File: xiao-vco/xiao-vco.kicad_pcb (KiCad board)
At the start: 2 copper layers, 38 x 100 mm, 52 parts, among them J1 C2M, J2 C2F, J3 Eurorack Power, J4 CV1, J5 V/OCT, J6 OUT, J7 CV2, J8 C1M, J9 C1F, U1 SeeeduinoXIAO, U2 MCP6004, U3 LM4040DBZ-10, U4 TL072, U5 LM1117-5.0

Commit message: First completed routing
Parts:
- removed the mouse-bite-2mm-slot at (169.0, 100.0)
- RV1: footprint Potentiometer_THT:Potentiometer_Alpha_RD901F-40-00D_Single_Vertical -> Personal:Potentiometer_Alpha_RD901F-40-00D_Single_Vertical-Hanging
- mouse-bite-2mm-slot (x2): footprint Panelization:mouse-bite-2mm-slot -> Personal:Mouse_bite_2x5mm
- moved R11 31.7 mm to (179.0, 121.5), turned to 180 degrees
- moved C6 13.2 mm to (184.8, 89.3), turned to -90 degrees
- moved C10 9.54 mm to (175.9, 86.9), turned to 0 degrees
- moved R9 8.02 mm to (175.1, 100.2), turned to 0 degrees
- moved C8 6.49 mm to (175.1, 97.9), turned to 0 degrees
- moved U4 6.10 mm to (176.9, 92.3), turned to 90 degrees
- moved mouse-bite-2mm-slot 6.00 mm to (169.0, 60.0)
- moved mouse-bite-2mm-slot 5.00 mm to (169.0, 140.0)
- moved R5 4.81 mm to (178.7, 100.2), turned to 180 degrees
- moved C7 4.13 mm to (182.5, 125.3), turned to -90 degrees
- moved C11 3.18 mm to (181.2, 94.3), turned to -90 degrees
- moved R4 2.25 mm to (175.3, 125.3)
- moved R8 2.15 mm to (178.7, 97.9), turned to 0 degrees
- moved U3 0.60 mm to (178.9, 125.3), turned to 180 degrees
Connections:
- C1 pad 2: GND -> GND1
- C2 pad 2: GND -> GND1
- C3 pad 2: GND -> GND1
- C4 pad 2: GND -> GND1
- J2 pad 1: GND -> GND1
- J4 pad S: GND -> GND1
- J5 pad S: GND -> GND1
- J6 pad S: GND -> GND1
- J7 pad S: GND -> GND1
- J9 pad 1: GND -> GND1
- RV1 pad 1: GND -> GND1
- RV2 pad 1: GND -> GND1
- RV3 pad 1: GND -> GND1
- RV4 pad 1: GND -> GND1
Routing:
- net +12V: track 0.07 -> 95.2 mm, vias 0 -> 1
- net -12V: track 2.18 -> 65.6 mm
- net +3V3: track 15.6 -> 58.4 mm, vias 0 -> 1
- net /CV1_IN: track 7.09 -> 44.1 mm, vias 0 -> 1
- net Net-(C8-Pad1): track 0.00 -> 36.4 mm, vias 0 -> 2
- net /CV2_IN: track 8.94 -> 43.1 mm, vias 0 -> 1
- net /AUDIO_OUT: track 0.00 -> 31.6 mm, vias 0 -> 1
- net +5V: track 0.00 -> 27.5 mm, vias 0 -> 1
- net /VOCT_IN: track 4.77 -> 26.0 mm, vias 0 -> 1
- net GND: track 17.1 -> 0.07 mm, vias 1 -> 16
- net GND1: track 0.00 -> 14.3 mm, vias 0 -> 19
- net Net-(C6-Pad2): track 0.00 -> 11.2 mm
- net Net-(C8-Pad2): track 0.00 -> 7.33 mm
- net /JACK_OUT: track 0.00 -> 2.87 mm
- net Net-(U4-Pad6): track 0.00 -> 1.27 mm
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- added copper zone on B.Cu, net GND1
- added copper zone on F.Cu, net GND1
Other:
- outline, holes or cut-outs redrawn

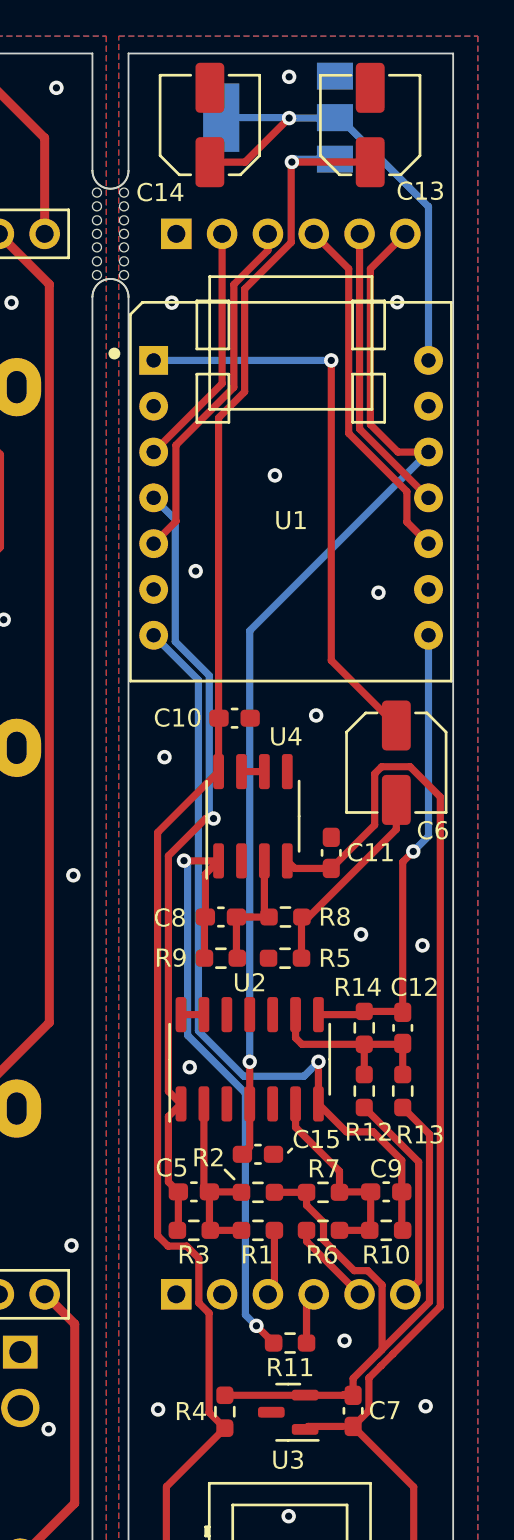
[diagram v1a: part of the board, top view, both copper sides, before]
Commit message: Routed all on one face
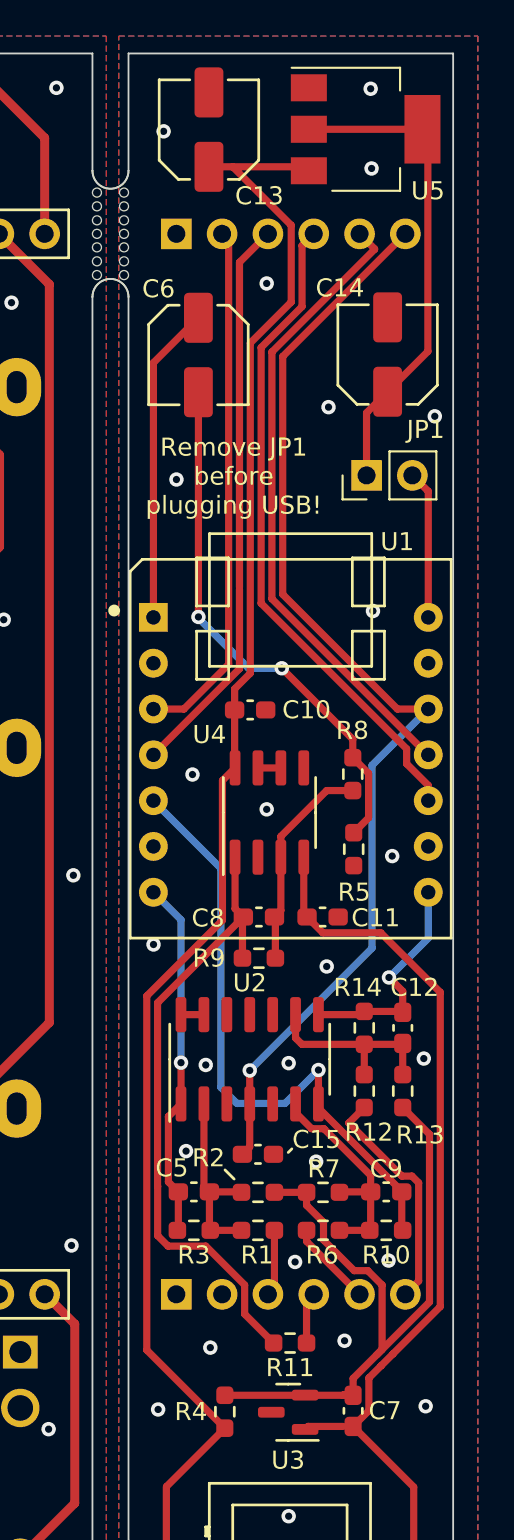
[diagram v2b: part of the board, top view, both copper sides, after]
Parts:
- added JP1: 5V, Connector_PinHeader_2.54mm:PinHeader_1x02_P2.54mm_Vertical, F.Cu at (183.2, 73.4)
- U5: moved to F.Cu
- moved C6 25.1 mm to (173.9, 66.7)
- moved C14 16.1 mm to (184.4, 66.7)
- moved U1 14.2 mm to (179.0, 88.9)
- moved C13 8.94 mm to (174.5, 54.2)
- moved R8 8.76 mm to (182.4, 90.0), turned to 90 degrees
- moved R5 7.14 mm to (182.5, 94.1), turned to -90 degrees
- moved U5 4.89 mm to (183.1, 54.2), turned to 0 degrees
- moved C11 3.59 mm to (180.8, 97.9), turned to 180 degrees
- moved C8 2.11 mm to (177.2, 97.9)
- moved R9 2.11 mm to (177.2, 100.2)
- moved C10 0.98 mm to (176.7, 86.4)
- moved U4 0.94 mm to (177.8, 92.1)
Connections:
- U1 pad 14: +5V -> Net-(U1-Pad14)
- U1 pad 4: /CV1_IN -> /POT3_IN
- U1 pad 5: /POT3_IN -> /CV2_IN
- U1 pad 7: /CV2_IN -> /CV1_IN
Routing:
- net /CV1_IN: track 44.1 -> 19.9 mm
- net /POT1_IN: track 16.2 -> 35.2 mm
- net Net-(C6-Pad2): track 11.2 -> 29.8 mm, vias 0 -> 2
- net /POT2_IN: track 19.8 -> 36.5 mm
- net /POT4_IN: track 13.7 -> 29.2 mm
- net /AUDIO_OUT: track 31.6 -> 17.6 mm, vias 1 -> 0
- net /VOCT_IN: track 26.0 -> 12.4 mm
- net -12V: track 65.6 -> 53.9 mm
- net /POT3_IN: track 19.8 -> 31.4 mm
- net /CV2_IN: track 43.1 -> 34.8 mm
- net Net-(U1-Pad14): track 0.00 -> 8.24 mm
- net Net-(C8-Pad2): track 7.33 -> 12.0 mm
- net +3V3: track 58.4 -> 63.0 mm
- net Net-(C8-Pad1): track 36.4 -> 35.3 mm, vias 2 -> 0
- net Net-(C9-Pad1): track 11.5 -> 12.6 mm
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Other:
- board text added: "CV1"
- board text added: "CV2"
- board text added: "OUT"
- board text added: "Remove JP1 before plugging USB!"
- board text added: "V/ OCT"

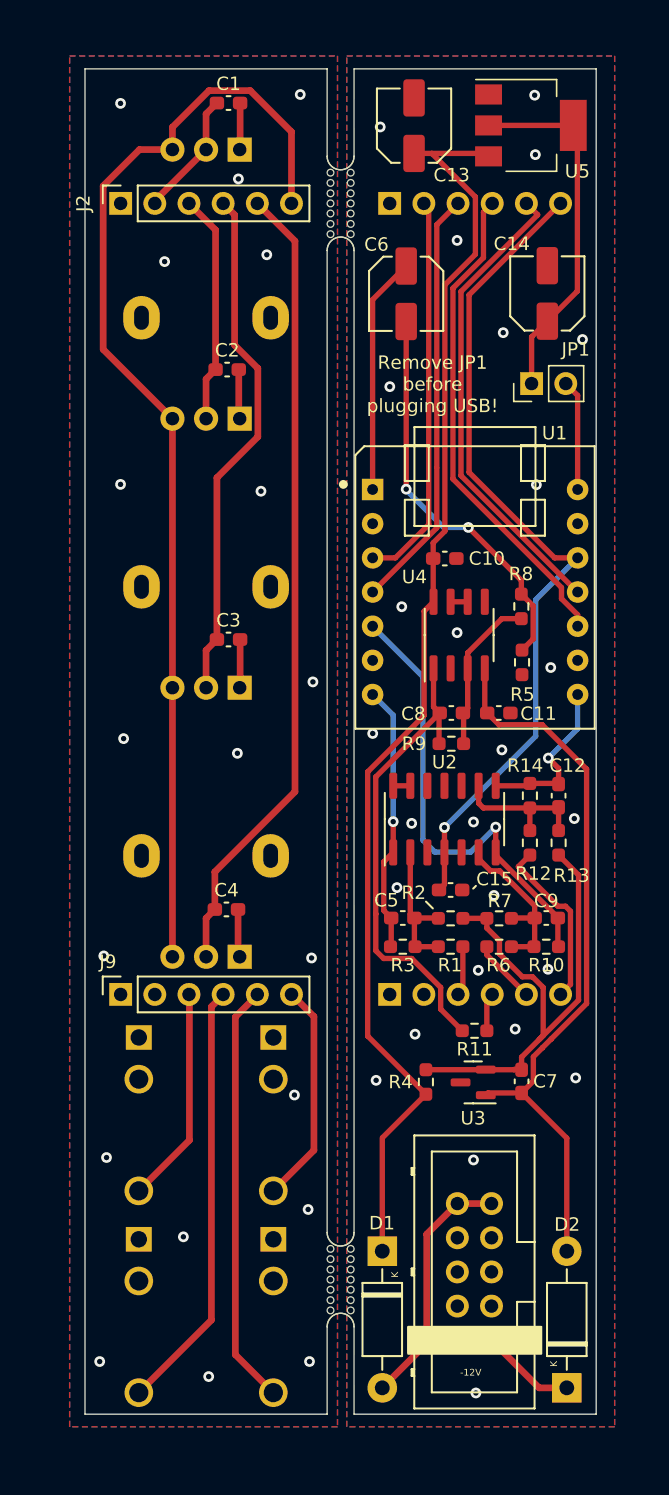
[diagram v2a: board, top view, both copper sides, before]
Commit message: Components now face inwards
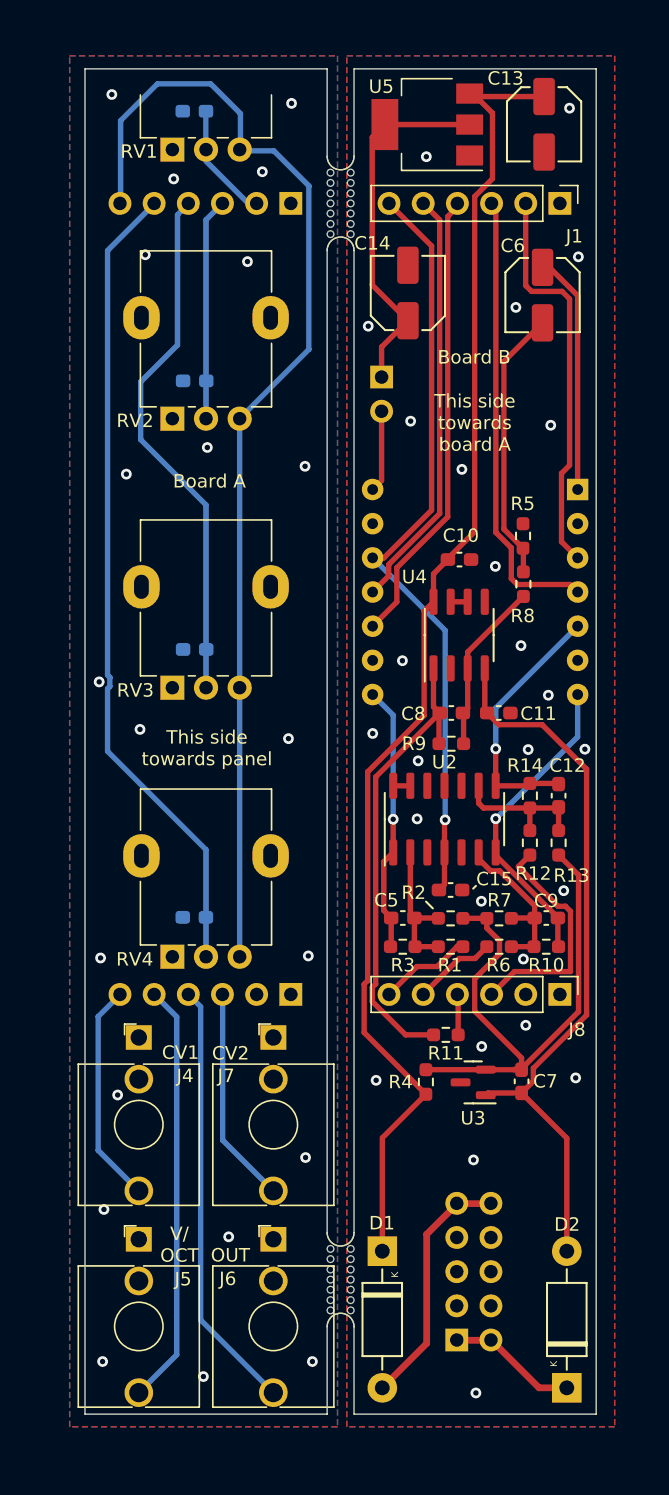
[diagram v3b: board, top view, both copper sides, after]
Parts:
- C1, C2, C3, C4, J2, J3, J9, JP1, U1: moved to B.Cu
- J1, J4, J5, J6, J7, J8, RV1, RV2, RV3, RV4: moved to F.Cu
- moved J1 12.7 mm to (185.3, 60.0)
- moved J2 12.7 mm to (165.3, 60.0)
- moved J8 12.7 mm to (185.3, 118.8)
- moved J9 12.7 mm to (165.3, 118.8)
- moved JP1 11.2 mm to (172.0, 72.9), turned to 180 degrees
- moved C14 10.4 mm to (174.0, 66.7)
- moved C6 10.1 mm to (184.0, 66.8)
- moved J4 10.0 mm to (154.0, 122.0), turned to 0 degrees
- moved J5 10.0 mm to (154.0, 137.0), turned to 0 degrees
- moved J6 10.0 mm to (164.0, 137.0), turned to 0 degrees
- moved J7 10.0 mm to (164.0, 122.0), turned to 0 degrees
- moved C13 9.67 mm to (184.1, 54.1), turned to -90 degrees
- moved R5 9.40 mm to (182.6, 84.7), turned to 90 degrees
- moved U5 7.71 mm to (175.4, 54.1), turned to 180 degrees
- moved RV1 5.00 mm to (156.5, 56.0)
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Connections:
- net Net-(C2-Pad1) renamed /CONN_POT3
- net Net-(J2-Pad2) renamed /CONN_POT4
- net Net-(J2-Pad4) renamed /CONN_POT2
- net Net-(J2-Pad5) renamed /CONN_POT1
- net Net-(J2-Pad6) renamed /CONN_3V3
- net Net-(J4-PadT) renamed /CONN_CV1
- net Net-(J5-PadT) renamed /CONN_VOCT
- net Net-(J6-PadT) renamed /CONN_OUT
- net Net-(J7-PadT) renamed /CONN_CV2
- R1 pad 1: /JACK_CV2 -> /JACK_CV1
- R12 pad 1: /JACK_CV1 -> /JACK_CV2
- U1 pad 5: /CV2_IN -> /VOCT_IN
- U1 pad 7: /CV1_IN -> /CV2_IN
- U1 pad 8: /VOCT_IN -> /CV1_IN
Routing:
- net GND1: track 14.3 -> 0.00 mm, vias 19 -> 21
- net /JACK_CV2: track 3.70 -> 17.5 mm
- net /CV2_IN: track 34.8 -> 23.2 mm
- net Net-(C6-Pad2): track 29.8 -> 20.3 mm, vias 2 -> 0
- net /VOCT_IN: track 12.4 -> 18.9 mm
- net /JACK_CV1: track 13.0 -> 6.96 mm
- net +3V3: track 63.0 -> 57.1 mm
- net /POT1_IN: track 35.2 -> 31.5 mm
- net +12V: track 96.1 -> 99.1 mm
- net /VREF_-10: track 38.1 -> 40.5 mm
- net /POT2_IN: track 36.5 -> 34.0 mm
- net /POT3_IN: track 31.4 -> 33.8 mm
- net Net-(U1-Pad14): track 8.24 -> 6.09 mm
- net /CONN_3V3: track 83.9 -> 85.6 mm
- net /JACK_VOCT: track 4.76 -> 6.20 mm
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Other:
- board text added: "Board A"
- board text added: "Board B"
- board text added: "Red stripe down"
- board text added: "This side towards board A"
- board text added: "This side towards board B"
- board text added: "This side towards panel"
- board text added: "Xiao DVCO Paul Battley 2022 CC-BY-SA-4.0"

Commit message: Use SMD diodes
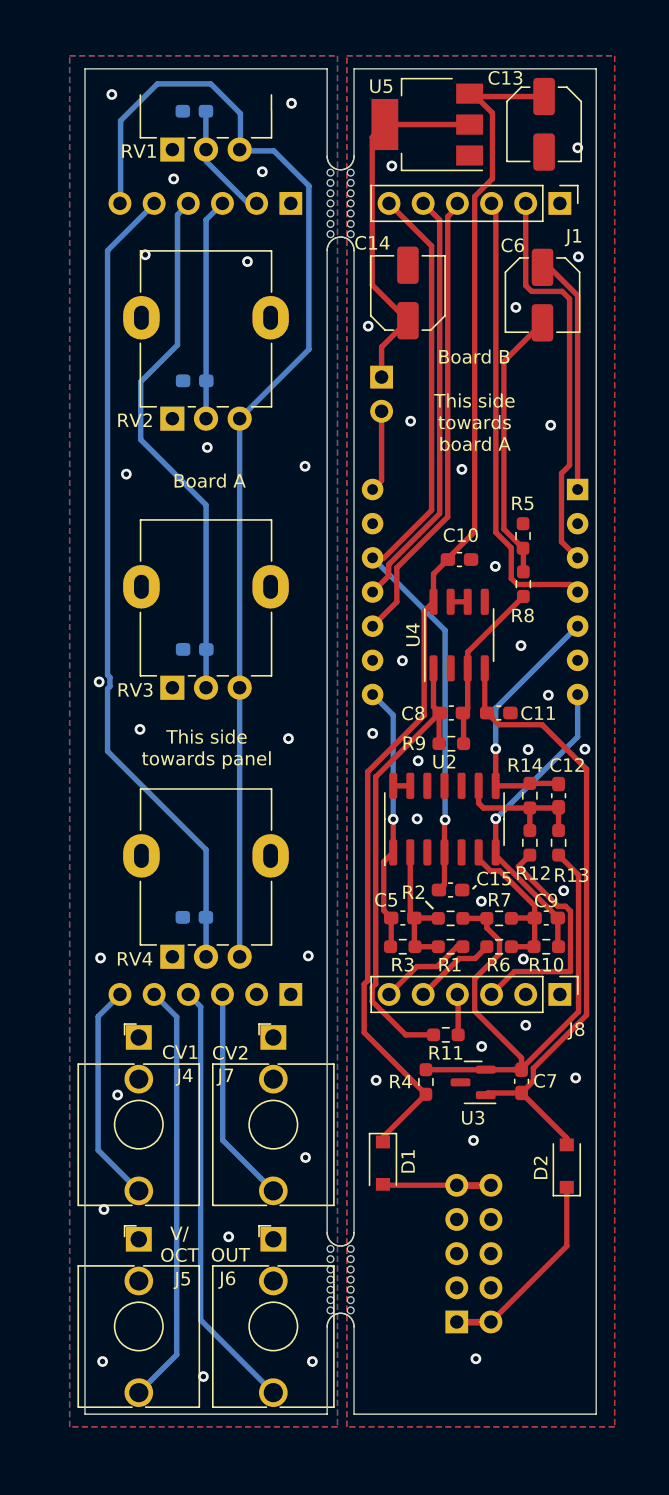
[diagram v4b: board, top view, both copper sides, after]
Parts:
- D1, D2: value 1N4001 -> SM4001; footprint Diode_THT:D_DO-41_SOD81_P10.16mm_Horizontal -> Personal:SOD-123FL
- J3: footprint Custom_Footprints:Eurorack_10_pin_header -> Personal:Eurorack_10_pin_header
- moved D2 16.5 mm to (185.8, 131.6)
- moved D1 6.54 mm to (172.1, 131.3)
- moved J3 1.34 mm to (177.6, 143.1)
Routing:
- net Net-(D1-Pad2): track 18.5 -> 8.03 mm
- net +12V: track 99.1 -> 91.0 mm
- net -12V: track 53.9 -> 45.9 mm
- net Net-(D2-Pad1): track 9.60 -> 14.8 mm
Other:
- board text added: "Module 5V supply jumper. Remove before plugging USB!"
- board text added: "Xiao DVCO Rev. 1 Paul Battley 2022 CC-BY-SA-4.0"
- board text removed: "Remove JP1 before plugging USB!"
- board text removed: "Xiao DVCO Paul Battley 2022 CC-BY-SA-4.0"

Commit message: Change MCP6004 to 6002 for availability
JLCPCB has MCP6002 in basic range.
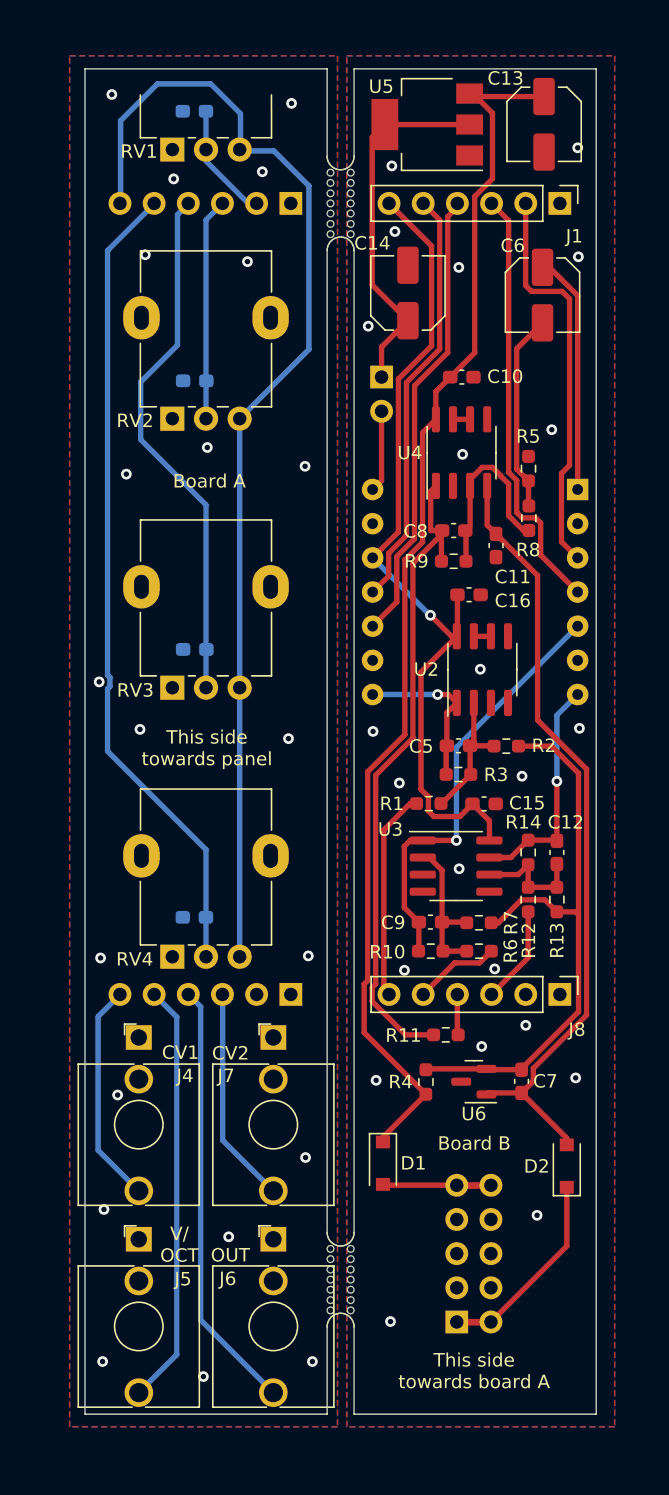
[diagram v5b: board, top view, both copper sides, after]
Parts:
- removed mouse-bite-2mm-slot (x2): VAL**, Personal:Mouse_bite_2x5mm
- added C16: 100n, Capacitor_SMD:C_0603_1608Metric_Pad1.08x0.95mm_HandSolder, F.Cu at (178.5, 89.1)
- added U6: LM4040DBZ-10, Package_TO_SOT_SMD:SOT-23, F.Cu at (178.9, 125.3)
- added mouse-bite-2x5mm: VAL**, Personal:Mouse_bite_2x5mm, F.Cu at (169.0, 60.0)
- added mouse-bite-2x5mm: VAL**, Personal:Mouse_bite_2x5mm, F.Cu at (169.0, 140.0)
- U2: value MCP6004 -> MCP6002-xSN; footprint Package_SO:SOIC-14_3.9x8.7mm_P1.27mm -> Package_SO:SOIC-8_3.9x4.9mm_P1.27mm
- U3: value LM4040DBZ-10 -> MCP6002-xSN; footprint Package_TO_SOT_SMD:SOT-23 -> Package_SO:SOIC-8_3.9x4.9mm_P1.27mm
- moved U3 16.1 mm to (177.6, 109.3), turned to 0 degrees
- moved C10 13.6 mm to (178.0, 72.9)
- moved C8 13.6 mm to (177.4, 84.3)
- moved R9 13.6 mm to (177.4, 86.6)
- moved U4 13.6 mm to (178.0, 78.5)
- moved R2 13.5 mm to (181.3, 100.3)
- moved R3 13.5 mm to (177.8, 102.5)
- moved C5 13.5 mm to (177.8, 100.3)
- moved C11 12.4 mm to (180.6, 85.4), turned to 90 degrees
- moved U2 11.5 mm to (179.5, 94.7)
- moved R1 10.8 mm to (175.6, 104.6), turned to 0 degrees
- moved C9 8.62 mm to (175.7, 113.4), turned to 180 degrees
- moved R10 8.59 mm to (175.7, 115.6), turned to 180 degrees
- moved C15 6.87 mm to (179.7, 104.6)
- moved R5 5.02 mm to (183.0, 79.7)
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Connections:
- U1 pad 5: /VOCT_IN -> /CV2_IN
- U1 pad 7: /CV2_IN -> /VOCT_IN
- U2 pad 4: +3V3 -> GND
- U2 pad 6: Net-(C9-Pad1) -> Net-(U2-Pad6)
- U2 pad 7: /CV2_IN -> Net-(U2-Pad6)
- U2 pad 8: /VOCT_IN -> +3V3
- U3 pad 1: -12V -> /CV2_IN
- U3 pad 2: /VREF_-10 -> Net-(C9-Pad1)
- U3 pad 3: (no net) -> GND
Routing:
- net Net-(C8-Pad1): track 34.8 -> 49.3 mm
- net -12V: track 45.9 -> 58.3 mm
- net /JACK_CV2: track 17.5 -> 7.27 mm
- net /JACK_CV1: track 6.96 -> 15.7 mm
- net /CV2_IN: track 23.2 -> 32.0 mm
- net /CV1_IN: track 19.9 -> 12.2 mm
- net +3V3: track 57.1 -> 62.6 mm
- net Net-(C6-Pad2): track 20.3 -> 14.8 mm
- net /VREF_-10: track 40.5 -> 43.8 mm
- net Net-(C12-Pad1): track 10.8 -> 8.73 mm
- net /VOCT_IN: track 18.9 -> 17.1 mm
- net /POT3_IN: track 33.8 -> 32.1 mm
- net Net-(U2-Pad13): track 1.27 -> 0.00 mm
- net Net-(U2-Pad6): track 0.00 -> 1.27 mm
- net Net-(C9-Pad1): track 12.6 -> 11.5 mm
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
